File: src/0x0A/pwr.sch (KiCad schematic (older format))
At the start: 20 parts

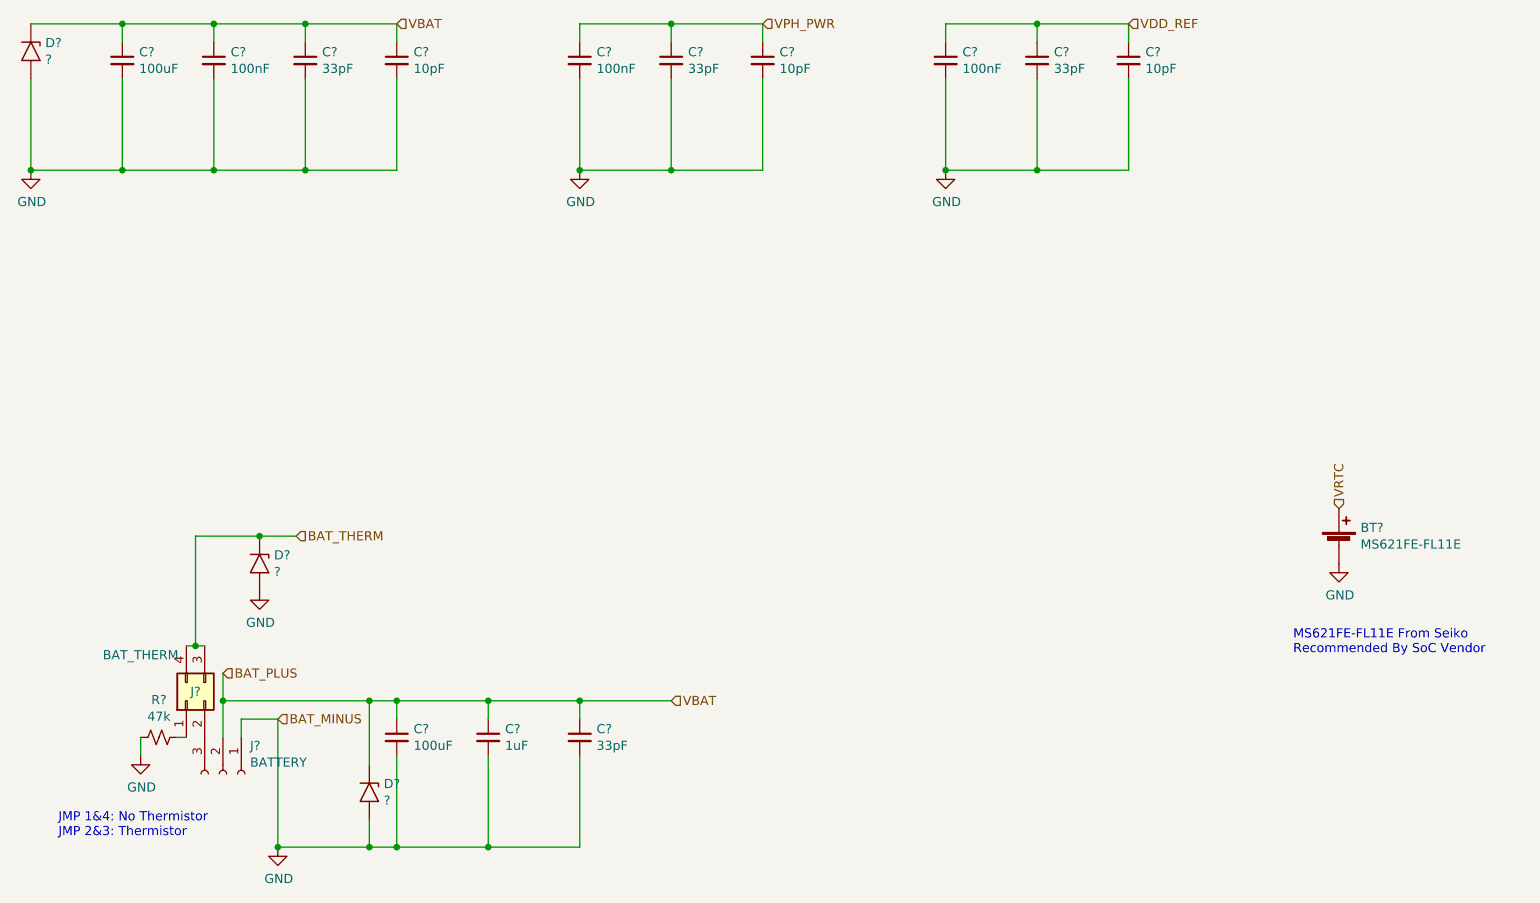
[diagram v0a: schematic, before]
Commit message: new file:   imgs/better.png 	modified:   src/0x0A/0x0A-cache.lib 	modified:   src/0x0A/0x0A.sch 	modified:   src/0x0A/antenna.sch 	modified:   src/0x0A/audio.sch 	modified:   src/0x0A/buttons.sch 	new file:   src/0x0A/cameras.sch 	modified:   src/0x0A/display.sch 	modified:   src/0x0A/gpio.sch 	modified:   src/0x0A/pwr.sch 	modified:   src/0x0A/sensors.sch 	modified:   src/0x0A/sim.sch 	modified:   src/0x0A/uart.sch 	modified:   src/0x0A/usb.sch 	new file:   src/models/body.obj 	new file:   src/models/phone.FCStd 	new file:   src/models/screen.obj
Added 3D models, integrated front & rear cameras, flash light, reformatting & more
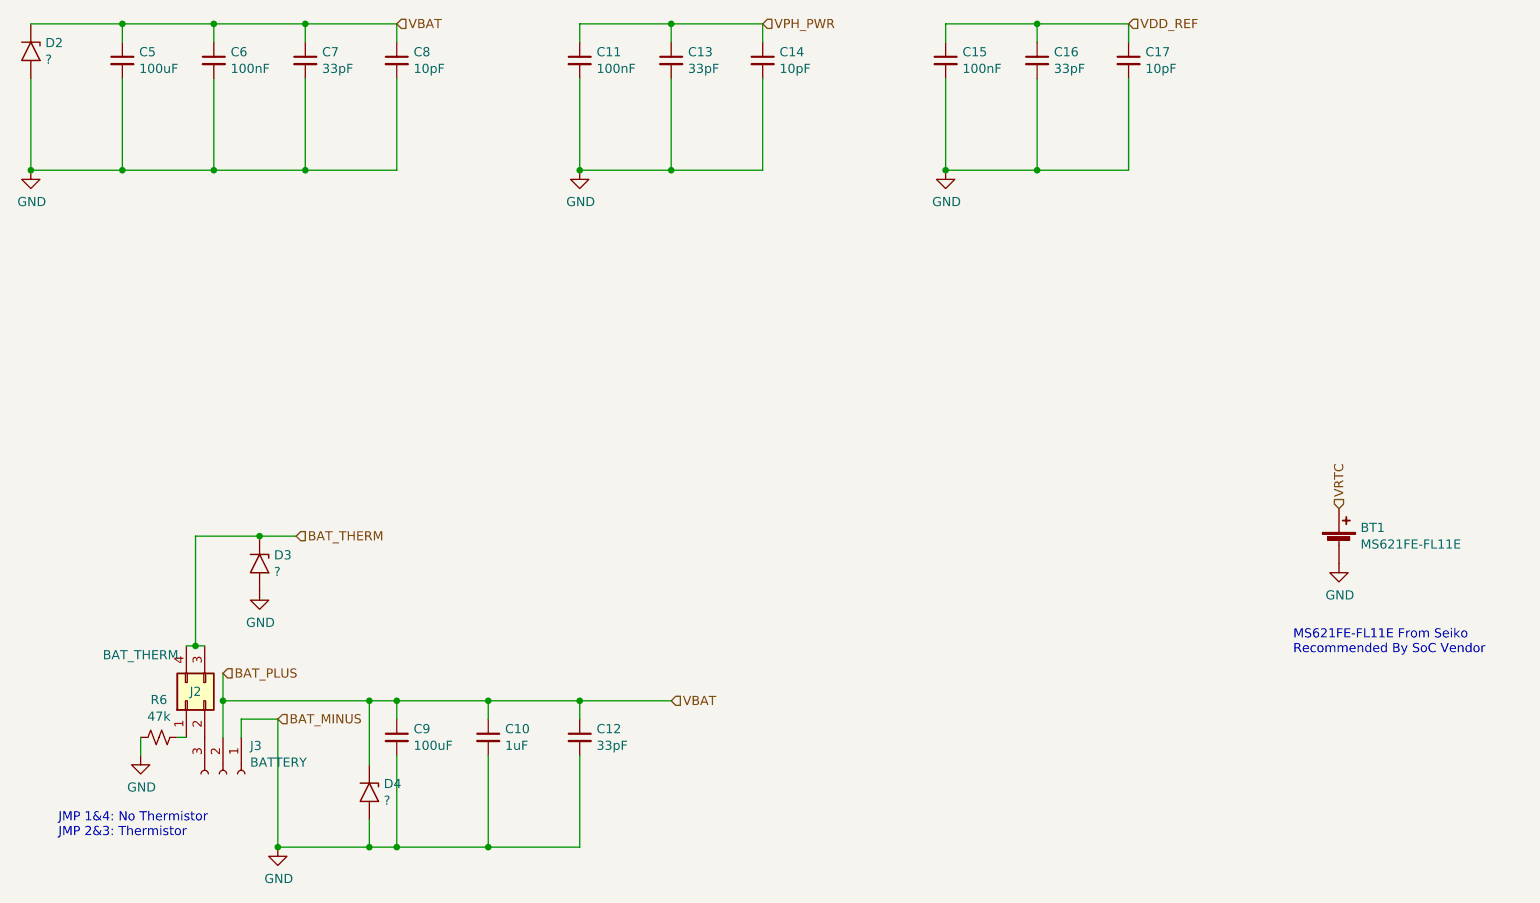
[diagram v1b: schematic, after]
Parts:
- C10, C11, C12, C13, C14, C15, C16, C17, C5, C6, C7, C8, C9: renamed from C?; footprint (none) -> Capacitor_SMD:C_0603_1608Metric
- R6: renamed from R?; footprint (none) -> Resistor_SMD:R_0402_1005Metric
- gave numbers to parts that had none: 6
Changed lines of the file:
@@
 $Descr A4 11693 8268
 encoding utf-8
-Sheet 6 12
+Sheet 5 13
 Title "0x0A SmartPhone"
 Date "2022-09-01"
 Rev "1"
 Comp "HackThisPhone.com"
-Comment1 ""
+Comment1 "Designed By @NoahGWood for"
 Comment2 ""
 Comment3 ""
@@
 $EndDescr
 $Comp
-L Device:C_Small C?
+L Device:C_Small C5
 U 1 1 631251E8
 P 1800 1800
-F 0 "C?" H 1892 1846 50  0000 L CNN
+F 0 "C5" H 1892 1846 50  0000 L CNN
 F 1 "100uF" H 1892 1755 50  0000 L CNN
-F 2 "" H 1800 1800 50  0001 C CNN
+F 2 "Capacitor_SMD:C_0603_1608Metric" H 1800 1800 50  0001 C CNN
 F 3 "~" H 1800 1800 50  0001 C CNN
 	1    1800 1800
@@
 $EndComp
 $Comp
-L Device:C_Small C?
+L Device:C_Small C6
 U 1 1 631254CA
 P 2300 1800
-F 0 "C?" H 2392 1846 50  0000 L CNN
+F 0 "C6" H 2392 1846 50  0000 L CNN
 F 1 "100nF" H 2392 1755 50  0000 L CNN
-F 2 "" H 2300 1800 50  0001 C CNN
+F 2 "Capacitor_SMD:C_0603_1608Metric" H 2300 1800 50  0001 C CNN
 F 3 "~" H 2300 1800 50  0001 C CNN
 	1    2300 1800
@@
 $EndComp
 $Comp
-L Device:C_Small C?
+L Device:C_Small C7
 U 1 1 6312556C
 P 2800 1800
-F 0 "C?" H 2892 1846 50  0000 L CNN
+F 0 "C7" H 2892 1846 50  0000 L CNN
 F 1 "33pF" H 2892 1755 50  0000 L CNN
-F 2 "" H 2800 1800 50  0001 C CNN
+F 2 "Capacitor_SMD:C_0603_1608Metric" H 2800 1800 50  0001 C CNN
 F 3 "~" H 2800 1800 50  0001 C CNN
 	1    2800 1800
@@
 $EndComp
 $Comp
-L Device:C_Small C?
+L Device:C_Small C8
 U 1 1 63125639
 P 3300 1800
-F 0 "C?" H 3392 1846 50  0000 L CNN
+F 0 "C8" H 3392 1846 50  0000 L CNN
 F 1 "10pF" H 3392 1755 50  0000 L CNN
-F 2 "" H 3300 1800 50  0001 C CNN
+F 2 "Capacitor_SMD:C_0603_1608Metric" H 3300 1800 50  0001 C CNN
 F 3 "~" H 3300 1800 50  0001 C CNN
 	1    3300 1800
@@
 $EndComp
 $Comp
-L Diode:1.5KExxA D?
+L Diode:1.5KExxA D2
 U 1 1 63126453
 P 1300 1750
-F 0 "D?" V 1254 1829 50  0000 L CNN
+F 0 "D2" V 1254 1829 50  0000 L CNN
 F 1 "?" V 1345 1829 50  0000 L CNN
 F 2 "Diode_THT:D_DO-201AE_P15.24mm_Horizontal" H 1300 1550 50  0001 C CNN
@@
 $EndComp
 $Comp
-L Device:C_Small C?
+L Device:C_Small C11
 U 1 1 63128108
 P 4300 1800
-F 0 "C?" H 4392 1846 50  0000 L CNN
+F 0 "C11" H 4392 1846 50  0000 L CNN
 F 1 "100nF" H 4392 1755 50  0000 L CNN
-F 2 "" H 4300 1800 50  0001 C CNN
+F 2 "Capacitor_SMD:C_0603_1608Metric" H 4300 1800 50  0001 C CNN
 F 3 "~" H 4300 1800 50  0001 C CNN
 	1    4300 1800
@@
 $EndComp
 $Comp
-L Device:C_Small C?
+L Device:C_Small C13
 U 1 1 6312810E
 P 4800 1800
-F 0 "C?" H 4892 1846 50  0000 L CNN
+F 0 "C13" H 4892 1846 50  0000 L CNN
 F 1 "33pF" H 4892 1755 50  0000 L CNN
-F 2 "" H 4800 1800 50  0001 C CNN
+F 2 "Capacitor_SMD:C_0603_1608Metric" H 4800 1800 50  0001 C CNN
 F 3 "~" H 4800 1800 50  0001 C CNN
 	1    4800 1800
@@
 $EndComp
 $Comp
-L Device:C_Small C?
+L Device:C_Small C14
 U 1 1 63128114
 P 5300 1800
-F 0 "C?" H 5392 1846 50  0000 L CNN
+F 0 "C14" H 5392 1846 50  0000 L CNN
 F 1 "10pF" H 5392 1755 50  0000 L CNN
-F 2 "" H 5300 1800 50  0001 C CNN
+F 2 "Capacitor_SMD:C_0603_1608Metric" H 5300 1800 50  0001 C CNN
 F 3 "~" H 5300 1800 50  0001 C CNN
 	1    5300 1800
@@
 $EndComp
 $Comp
-L Device:C_Small C?
+L Device:C_Small C15
 U 1 1 631284A6
 P 6300 1800
-F 0 "C?" H 6392 1846 50  0000 L CNN
+F 0 "C15" H 6392 1846 50  0000 L CNN
 F 1 "100nF" H 6392 1755 50  0000 L CNN
-F 2 "" H 6300 1800 50  0001 C CNN
+F 2 "Capacitor_SMD:C_0603_1608Metric" H 6300 1800 50  0001 C CNN
 F 3 "~" H 6300 1800 50  0001 C CNN
 	1    6300 1800
@@
 $EndComp
 $Comp
-L Device:C_Small C?
+L Device:C_Small C16
 U 1 1 631284AC
 P 6800 1800
-F 0 "C?" H 6892 1846 50  0000 L CNN
+F 0 "C16" H 6892 1846 50  0000 L CNN
 F 1 "33pF" H 6892 1755 50  0000 L CNN
-F 2 "" H 6800 1800 50  0001 C CNN
+F 2 "Capacitor_SMD:C_0603_1608Metric" H 6800 1800 50  0001 C CNN
 F 3 "~" H 6800 1800 50  0001 C CNN
 	1    6800 1800
@@
 $EndComp
 $Comp
-L Device:C_Small C?
+L Device:C_Small C17
 U 1 1 631284B2
 P 7300 1800
-F 0 "C?" H 7392 1846 50  0000 L CNN
+F 0 "C17" H 7392 1846 50  0000 L CNN
 F 1 "10pF" H 7392 1755 50  0000 L CNN
-F 2 "" H 7300 1800 50  0001 C CNN
+F 2 "Capacitor_SMD:C_0603_1608Metric" H 7300 1800 50  0001 C CNN
 F 3 "~" H 7300 1800 50  0001 C CNN
 	1    7300 1800
@@
 $EndComp
 $Comp
-L power:GND #PWR?
+L power:GND #PWR0107
 U 1 1 631287FD
 P 1300 2400
-F 0 "#PWR?" H 1300 2150 50  0001 C CNN
+F 0 "#PWR0107" H 1300 2150 50  0001 C CNN
 F 1 "GND" H 1305 2227 50  0000 C CNN
 F 2 "" H 1300 2400 50  0001 C CNN
@@
 Connection ~ 1300 2400
 $Comp
-L power:GND #PWR?
+L power:GND #PWR0108
 U 1 1 6312F0B0
 P 4300 2400
-F 0 "#PWR?" H 4300 2150 50  0001 C CNN
+F 0 "#PWR0108" H 4300 2150 50  0001 C CNN
 F 1 "GND" H 4305 2227 50  0000 C CNN
 F 2 "" H 4300 2400 50  0001 C CNN
@@
 	6800 2400 6300 2400
 $Comp
-L power:GND #PWR?
+L power:GND #PWR0109
 U 1 1 63130CD9
 P 6300 2400
-F 0 "#PWR?" H 6300 2150 50  0001 C CNN
+F 0 "#PWR0109" H 6300 2150 50  0001 C CNN
 F 1 "GND" H 6305 2227 50  0000 C CNN
 F 2 "" H 6300 2400 50  0001 C CNN
@@
 Connection ~ 6300 2400
 $Comp
-L Connector_Generic:Conn_02x02_Counter_Clockwise J?
+L Connector_Generic:Conn_02x02_Counter_Clockwise J2
 U 1 1 6313A44E
 P 2150 5300
-F 0 "J?" V 2200 5250 50  0000 C CNN
+F 0 "J2" V 2200 5250 50  0000 C CNN
 F 1 "BAT_THERM" V 2400 5550 50  0000 C CNN
 F 2 "" H 2150 5300 50  0001 C CNN
@@
 	1900 5600 1900 5500
 $Comp
-L Device:R_Small_US R?
+L Device:R_Small_US R6
 U 1 1 6313DA98
 P 2000 5500
-F 0 "R?" V 1795 5500 50  0000 C CNN
+F 0 "R6" V 1795 5500 50  0000 C CNN
 F 1 "47k" V 1886 5500 50  0000 C CNN
-F 2 "" H 2000 5500 50  0001 C CNN
+F 2 "Resistor_SMD:R_0402_1005Metric" H 2000 5500 50  0001 C CNN
 F 3 "~" H 2000 5500 50  0001 C CNN
 	1    2000 5500
@@
 $EndComp
 $Comp
-L power:GND #PWR?
+L power:GND #PWR0110
 U 1 1 6313CADC
 P 1900 5600
-F 0 "#PWR?" H 1900 5350 50  0001 C CNN
+F 0 "#PWR0110" H 1900 5350 50  0001 C CNN
 F 1 "GND" H 1905 5427 50  0000 C CNN
 F 2 "" H 1900 5600 50  0001 C CNN
@@
 	2450 5400 2650 5400
 $Comp
-L Connector:Conn_01x03_Female J?
+L Connector:Conn_01x03_Female J3
 U 1 1 6316E961
 P 2350 5700
-F 0 "J?" V 2196 5848 50  0000 L CNN
+F 0 "J3" V 2196 5848 50  0000 L CNN
 F 1 "BATTERY" V 2287 5848 50  0000 L CNN
 F 2 "" H 2350 5700 50  0001 C CNN
@@
 $EndComp
 $Comp
-L Device:Battery_Cell BT?
+L Device:Battery_Cell BT1
 U 1 1 6322406B
 P 8450 4450
-F 0 "BT?" H 8568 4546 50  0000 L CNN
+F 0 "BT1" H 8568 4546 50  0000 L CNN
 F 1 "MS621FE-FL11E" H 8568 4455 50  0000 L CNN
 F 2 "" V 8450 4510 50  0001 C CNN
@@
 $EndComp
 $Comp
-L power:GND #PWR?
+L power:GND #PWR0111
 U 1 1 63224D9C
 P 8450 4550
-F 0 "#PWR?" H 8450 4300 50  0001 C CNN
+F 0 "#PWR0111" H 8450 4300 50  0001 C CNN
 F 1 "GND" H 8455 4377 50  0000 C CNN
 F 2 "" H 8450 4550 50  0001 C CNN
@@
 JMP 1&4: No Thermistor\nJMP 2&3: Thermistor
 $Comp
-L Device:C_Small C?
+L Device:C_Small C9
 U 1 1 632447D8
 P 3300 5500
-F 0 "C?" H 3392 5546 50  0000 L CNN
+F 0 "C9" H 3392 5546 50  0000 L CNN
 F 1 "100uF" H 3392 5455 50  0000 L CNN
-F 2 "" H 3300 5500 50  0001 C CNN
+F 2 "Capacitor_SMD:C_0603_1608Metric" H 3300 5500 50  0001 C CNN
 F 3 "~" H 3300 5500 50  0001 C CNN
 	1    3300 5500
@@
 $EndComp
 $Comp
-L Device:C_Small C?
+L Device:C_Small C10
 U 1 1 63244CD6
 P 3800 5500
-F 0 "C?" H 3892 5546 50  0000 L CNN
+F 0 "C10" H 3892 5546 50  0000 L CNN
 F 1 "1uF" H 3892 5455 50  0000 L CNN
-F 2 "" H 3800 5500 50  0001 C CNN
+F 2 "Capacitor_SMD:C_0603_1608Metric" H 3800 5500 50  0001 C CNN
 F 3 "~" H 3800 5500 50  0001 C CNN
 	1    3800 5500
@@
 $EndComp
 $Comp
-L Device:C_Small C?
+L Device:C_Small C12
 U 1 1 63244E9B
 P 4300 5500
-F 0 "C?" H 4392 5546 50  0000 L CNN
+F 0 "C12" H 4392 5546 50  0000 L CNN
 F 1 "33pF" H 4392 5455 50  0000 L CNN
-F 2 "" H 4300 5500 50  0001 C CNN
+F 2 "Capacitor_SMD:C_0603_1608Metric" H 4300 5500 50  0001 C CNN
 F 3 "~" H 4300 5500 50  0001 C CNN
 	1    4300 5500
@@
 $EndComp
 $Comp
-L power:GND #PWR?
+L power:GND #PWR0112
 U 1 1 632475C7
 P 2650 6100
-F 0 "#PWR?" H 2650 5850 50  0001 C CNN
+F 0 "#PWR0112" H 2650 5850 50  0001 C CNN
 F 1 "GND" H 2655 5927 50  0000 C CNN
 F 2 "" H 2650 6100 50  0001 C CNN
@@
 	3300 5300 3800 5300
 $Comp
-L Diode:1.5KExxA D?
+L Diode:1.5KExxA D4
 U 1 1 6324DEEB
 P 3150 5800
-F 0 "D?" V 3104 5879 50  0000 L CNN
+F 0 "D4" V 3104 5879 50  0000 L CNN
 F 1 "?" V 3195 5879 50  0000 L CNN
 F 2 "Diode_THT:D_DO-201AE_P15.24mm_Horizontal" H 3150 5600 50  0001 C CNN
@@
 $EndComp
 $Comp
-L Diode:1.5KExxA D?
+L Diode:1.5KExxA D3
 U 1 1 6324F474
 P 2550 4550
-F 0 "D?" V 2504 4629 50  0000 L CNN
+F 0 "D3" V 2504 4629 50  0000 L CNN
 F 1 "?" V 2595 4629 50  0000 L CNN
 F 2 "Diode_THT:D_DO-201AE_P15.24mm_Horizontal" H 2550 4350 50  0001 C CNN
@@
 	2550 4400 2750 4400
 $Comp
-L power:GND #PWR?
+L power:GND #PWR0113
 U 1 1 63260B8E
 P 2550 4700
-F 0 "#PWR?" H 2550 4450 50  0001 C CNN
+F 0 "#PWR0113" H 2550 4450 50  0001 C CNN
 F 1 "GND" H 2555 4527 50  0000 C CNN
 F 2 "" H 2550 4700 50  0001 C CNN

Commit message: Updated schematics, started working on board layout
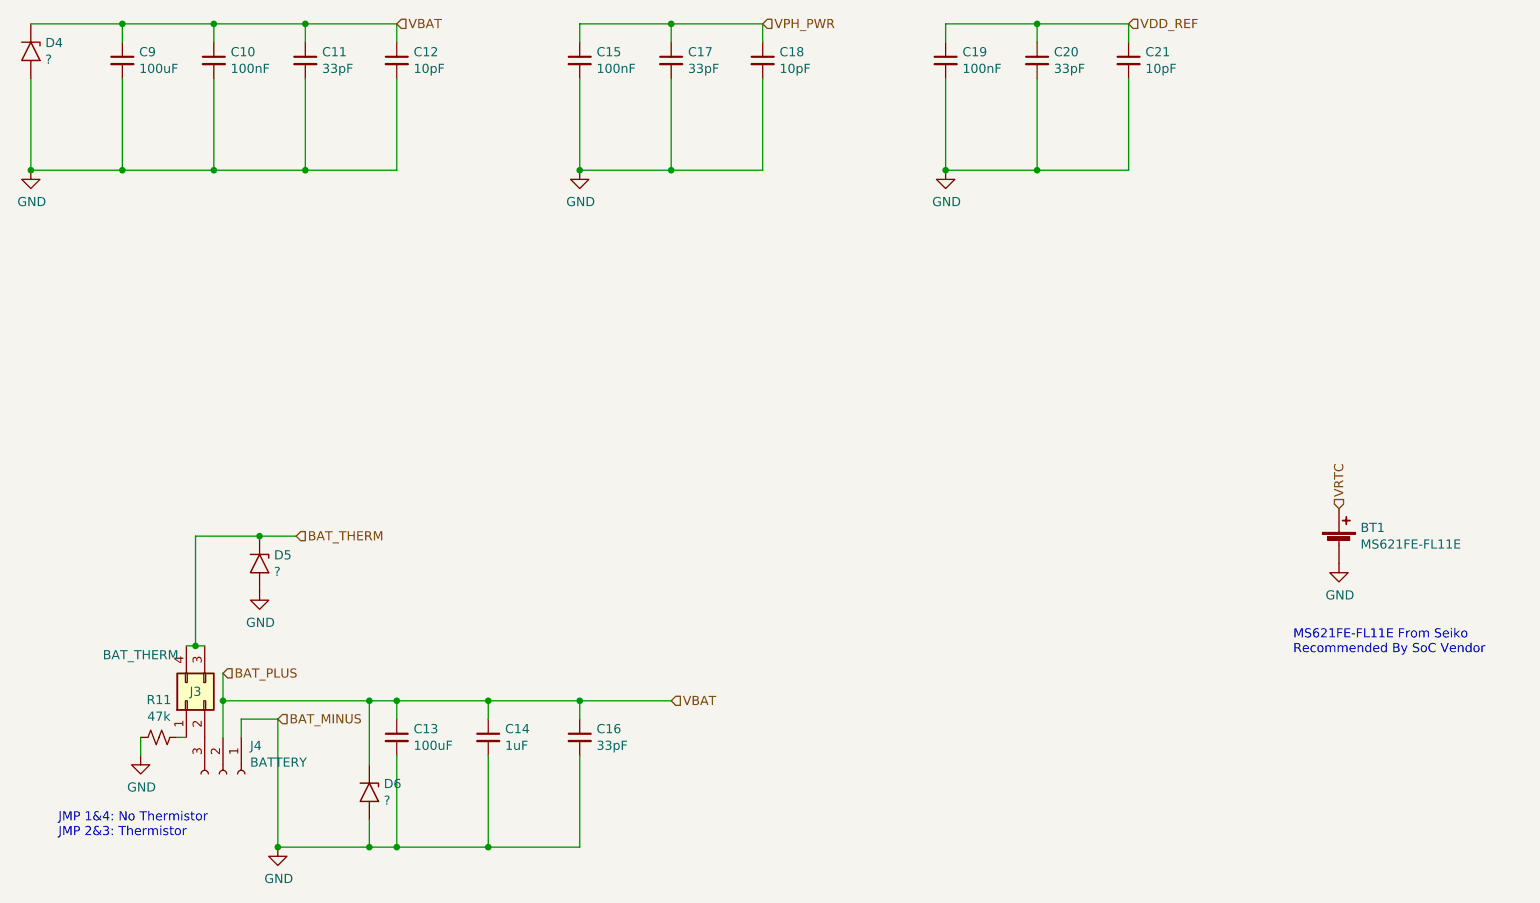
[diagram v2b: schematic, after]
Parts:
- removed C11: 100nF, Capacitor_SMD:C_0603_1608Metric, symbol Device:C_Small
- added C19: 100nF, Capacitor_SMD:C_0402_1005Metric, symbol Device:C_Small
- BT1: footprint (none) -> Battery:BatteryHolder_Seiko_MS621F
- C10: renamed from C6; footprint Capacitor_SMD:C_0603_1608Metric -> Capacitor_SMD:C_0402_1005Metric; LCSC Part # (none) -> C307331
- C11: renamed from C7; footprint Capacitor_SMD:C_0603_1608Metric -> Capacitor_SMD:C_0402_1005Metric; LCSC Part # (none) -> C1562
- C12: renamed from C8; footprint Capacitor_SMD:C_0603_1608Metric -> Capacitor_SMD:C_0402_1005Metric; LCSC Part # (none) -> C32949
- C13: renamed from C9; footprint Capacitor_SMD:C_0603_1608Metric -> Capacitor_SMD:C_1206_3216Metric; LCSC Part # (none) -> C15008
- C14: renamed from C10; LCSC Part # (none) -> C15849
- C15: footprint Capacitor_SMD:C_0603_1608Metric -> Capacitor_SMD:C_0402_1005Metric; LCSC Part # (none) -> C307331
- C16: renamed from C12; footprint Capacitor_SMD:C_0603_1608Metric -> Capacitor_SMD:C_0402_1005Metric; LCSC Part # (none) -> C1562
- C17: renamed from C13; footprint Capacitor_SMD:C_0603_1608Metric -> Capacitor_SMD:C_0402_1005Metric; LCSC Part # (none) -> C1562
- C18: renamed from C14; footprint Capacitor_SMD:C_0603_1608Metric -> Capacitor_SMD:C_0402_1005Metric; LCSC Part # (none) -> C32949
- C20: renamed from C16; footprint Capacitor_SMD:C_0603_1608Metric -> Capacitor_SMD:C_0402_1005Metric; LCSC Part # (none) -> C1562
- C21: renamed from C17; footprint Capacitor_SMD:C_0603_1608Metric -> Capacitor_SMD:C_0402_1005Metric; LCSC Part # (none) -> C32949
- C9: renamed from C5; footprint Capacitor_SMD:C_0603_1608Metric -> Capacitor_SMD:C_1206_3216Metric; LCSC Part # (none) -> C15008
- renumbered D2 to D4, D3 to D5, D4 to D6, J2 to J3, J3 to J4, R6 to R11
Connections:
- net GND: now also C19.2
- net VDD_REF: now also C19.1; no longer C15.1
- net VPH_PWR: now also C15.1
